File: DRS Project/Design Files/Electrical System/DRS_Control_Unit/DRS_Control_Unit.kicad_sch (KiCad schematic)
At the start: 32 parts, among them J1 Deutsch DT, J2 Servo, U1 AMS1117, U2 LM2596S-ADJ, U3 Teensy4.0-NU-Teams, U4 TJA1051T-3

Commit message: minor change
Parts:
- added F2: 3A, NU-Teams-Footprints:Fuseholder_Littelfuse_Nano2_154x, symbol Device:Fuse
- C1, C2: footprint (none) -> Capacitor_SMD:C_1206_3216Metric_Pad1.33x1.80mm_HandSolder
- D5, D6: value SS54 -> SS34; footprint (none) -> Diode_SMD:D_SMA_Handsoldering
- F1: footprint (none) -> NU-Teams-Footprints:Fuseholder_Littelfuse_Nano2_154x
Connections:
- net +6V: now also F2.1; no longer C2.2, C4.1, D7.2 (A), L1.2, R6.2, TP5.1
- new net: C2.2, C4.1, D7.2 (A), F2.2, L1.2, R6.2, TP5.1
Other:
- moved on the sheet: C1, C4, D1, D2, D3, D5, D7, F1, J1, J2, R1, R2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

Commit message: parts finalised
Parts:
- removed TP1: UNFUS, TestPoint:TestPoint_THTPad_D2.0mm_Drill1.0mm, symbol Connector:TestPoint
- removed TP2: FUSED, TestPoint:TestPoint_THTPad_D2.0mm_Drill1.0mm, symbol Connector:TestPoint
- added J3: Screw, TerminalBlock_Phoenix:TerminalBlock_Phoenix_MKDS-1,5-2_1x02_P5.00mm_Horizontal, symbol Connector:Screw_Terminal_01x02
- C3, C4: footprint (none) -> DRS_Library:PCAP_8x10-ELECT_NCA-M
- L1: footprint DRS_Library:Inductor_HCM1A1104V3 -> DRS_Library:IND_AMDLA1004S-330MT
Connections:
- net +12V: now also J3.1 (Pin_1)
- net GND: now also J3.2 (Pin_2)
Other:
- note added: "Testing Terminal"

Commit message: nearly finised circuit v1.1
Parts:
- added C2: 100u, Capacitor_SMD:C_1206_3216Metric_Pad1.33x1.80mm_HandSolder, symbol Device:C
- added C3: C4, Capacitor_SMD:C_1206_3216Metric_Pad1.33x1.80mm_HandSolder, symbol Device:C
- added C4: 10u, Capacitor_SMD:C_1206_3216Metric_Pad1.33x1.80mm_HandSolder, symbol Device:C
- added C5, C6: 22u, Capacitor_SMD:C_1206_3216Metric_Pad1.33x1.80mm_HandSolder, symbol Device:C
- added IC1: AP63301QWU-7, DRS_Library:TSOT-26, symbol AP63301QWU-7:AP63301QWU-7
- added L1: 4.7u, symbol Device:L
- added R5: 9k, Resistor_SMD:R_1206_3216Metric_Pad1.30x1.75mm_HandSolder, symbol Device:R
- added R6: 1k, Resistor_SMD:R_1206_3216Metric_Pad1.30x1.75mm_HandSolder, symbol Device:R
- added R7: R, Resistor_SMD:R_1206_3216Metric_Pad1.30x1.75mm_HandSolder, symbol Device:R
- C7: renamed from C2; now not fitted
- C8: renamed from C3; now not fitted
- C9: renamed from C4; now not fitted
- D6, D7, F2: now not fitted
- J3: renamed from J2; footprint Connector_PinHeader_2.54mm:PinHeader_1x03_P2.54mm_Vertical -> Connector_PinHeader_2.54mm:PinHeader_1x03_P2.54mm_Horizontal
- L2: renamed from L1; now not fitted
- R10: renamed from R7; now not fitted
- R8: renamed from R5; now not fitted
- R9: renamed from R6; now not fitted
- TP3: renamed from TP5; now not fitted
- TP4: renamed from TP6; now not fitted
- U4: renamed from U2; now not fitted
- renumbered J3 to J2, R4 to R1, R1 to R2, R2 to R3, R3 to R4, TP3 to TP1, TP4 to TP2, U3 to U2, U4 to U3
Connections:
- net +6V: now also C3.2, C5.1, L1.2, R6.2; no longer U1.3 (VI)
- net CAN HIGH: now also R7.1
- net CAN LOW: now also R7.2
- net GND: now also C4.2, C6.2, IC1.4 (GND), R5.1
- net SIGNAL: now also U2.19 (19_A5_SCL0); no longer U2.2 (2_OUT2)
- net VIN: now also U1.3 (VI), C4.1, IC1.2 (EN), IC1.3 (VIN)
- net at U2.0 (0_CAN2_RX): no longer U3.4 (RXD)
- net at U2.1 (1_CAN2_TX): no longer U3.1 (TXD)
- net at U2.22 (22_CAN1_TX): now also U3.1 (TXD)
- net at U2.23 (23_CAN1_RX): now also U3.4 (RXD)
- net at U3.5 (VIO): now also U2.VIN
- net +5V PROT: no longer names the net of D4.2 (A), D5.1 (K), U3.3 (VCC)
- net +5V PROT: no longer U2.VIN
- new net: C2.2, IC1.5 (SW), L1.1
- new net: C2.1, IC1.6 (BST)
- new net: C5.2, C6.1
- new net FB: C3.1, IC1.1 (FB), R5.2, R6.1
- no-connect marks 27 -> 26
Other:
- note added: "Servo Power Regulation v1"
- note added: "Servo Power Regulation v2"
- note removed: "Servo Power Regulation"
- moved on the sheet: C1, D1, D2, D3, D4, D5, F1, J1, J2, J3, R1, R2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

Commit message: update v1.1
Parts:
- added F3: 3A, NU-Teams-Footprints:Fuseholder_Littelfuse_Nano2_154x, symbol Device:Fuse
- C7, C8, C9, D6, D7, F2, L2, R10, R8, R9, TP3, TP4, U4: now left out of the parts list
- IC1: footprint DRS_Library:TSOT-26 -> DRS_Library:SOT95P280X100-6N
- L1: footprint (none) -> DRS_Library:IND_ASPI-0630LR_ABR-M
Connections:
- net +6V: now also F3.2; no longer C3.2, C5.1, L1.2, R6.2
- new net: C3.2, C5.1, F3.1, L1.2, R6.2
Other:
- moved on the sheet: C1, C2, C3, C4, C5, C6, D1, D2, D3, D4, D5, F1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

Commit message: more updates and sync
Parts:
- R5, R7: footprint Resistor_SMD:R_1206_3216Metric_Pad1.30x1.75mm_HandSolder -> Connector_PinSocket_2.54mm:PinSocket_1x02_P2.54mm_Vertical
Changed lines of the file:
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@@
 			)
 		)
-		(property "Footprint" "Resistor_SMD:R_1206_3216Metric_Pad1.30x1.75mm_HandSolder"
+		(property "Footprint" "Connector_PinSocket_2.54mm:PinSocket_1x02_P2.54mm_Vertical"
 			(at 98.552 101.6 90)
 			(hide yes)
@@
 			)
 		)
-		(property "Footprint" "Resistor_SMD:R_1206_3216Metric_Pad1.30x1.75mm_HandSolder"
+		(property "Footprint" "Connector_PinSocket_2.54mm:PinSocket_1x02_P2.54mm_Vertical"
 			(at 143.002 111.76 90)
 			(hide yes)

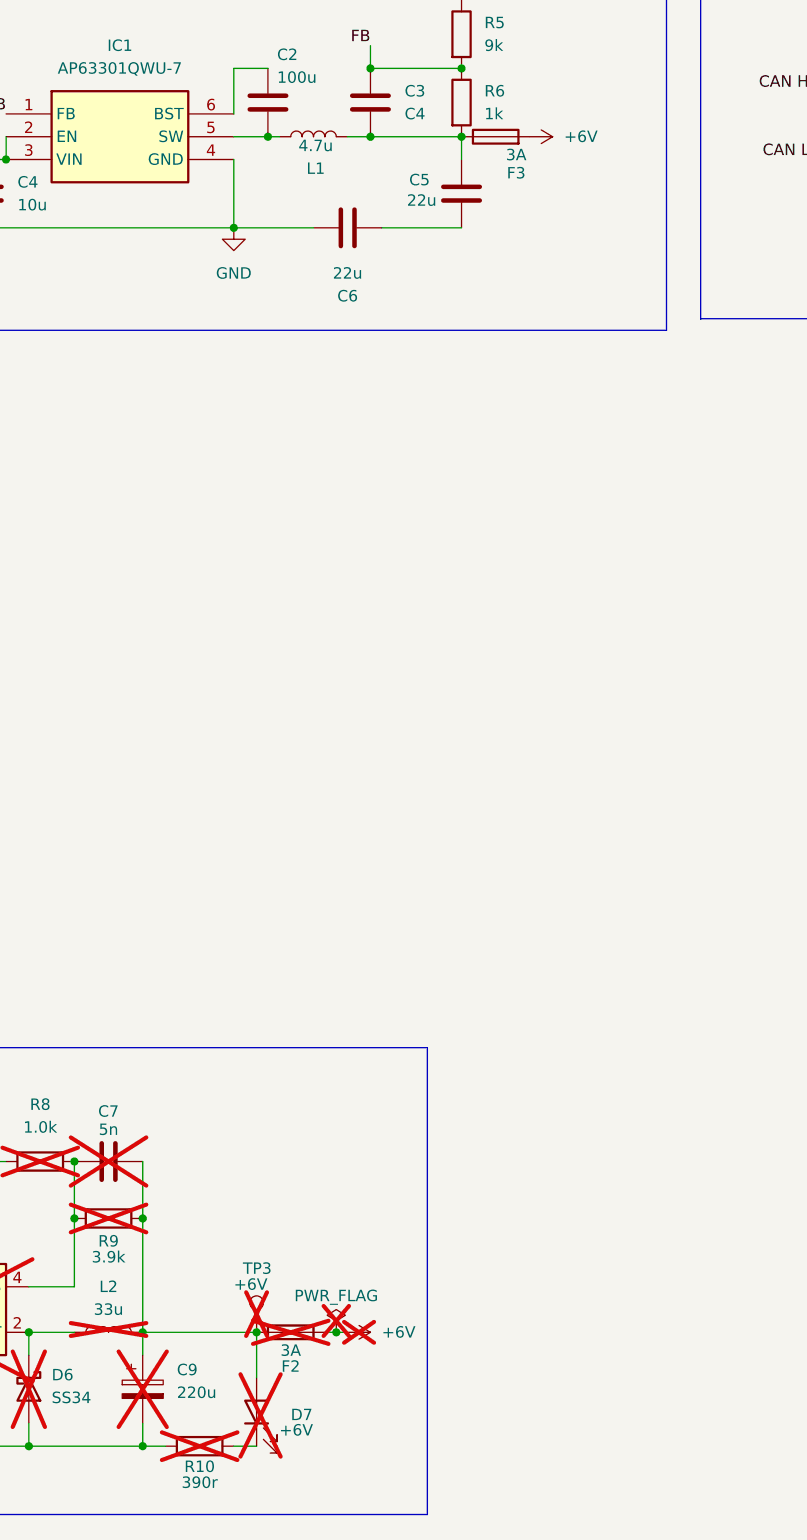
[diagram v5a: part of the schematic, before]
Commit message: added mounting and edgecut layer to pcb
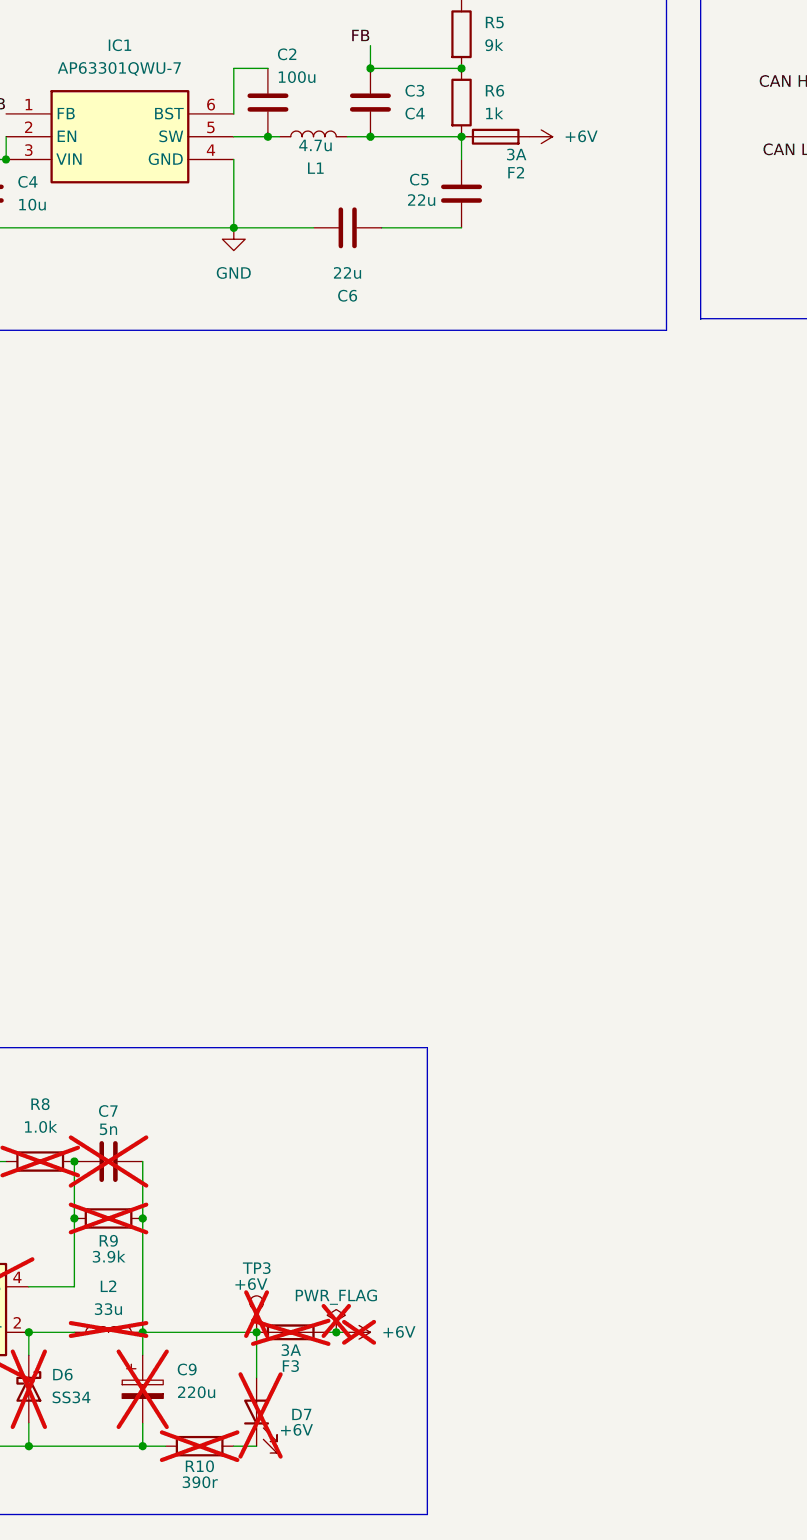
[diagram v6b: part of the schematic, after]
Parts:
- renumbered F3 to F2, F2 to F3
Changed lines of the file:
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@@
 		(in_pos_files no)
 		(dnp yes)
-		(property "Reference" "F2"
+		(property "Reference" "F3"
 			(at 81.28 250.19 90)
 			(show_name no)
@@
 			(project "DRS_Control_Unit"
 				(path "/63b578ff-1476-4f7d-9cf7-fea775e132b7"
-					(reference "F2")
+					(reference "F3")
 					(unit 1)
 				)
@@
 		(in_pos_files yes)
 		(dnp no)
-		(property "Reference" "F3"
+		(property "Reference" "F2"
 			(at 106.426 117.094 90)
 			(show_name no)
@@
 			(project "DRS_Control_Unit"
 				(path "/63b578ff-1476-4f7d-9cf7-fea775e132b7"
-					(reference "F3")
-					(unit 1)
-				)
+					(reference "F2")
+					(unit 1)
+				)
